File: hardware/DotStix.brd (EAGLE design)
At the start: 20.3 x 50 mm, 27 parts, among them IC2 SI1145, U1 ATMEGA328P-MU-QFN32, U2 TMP102

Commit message: Draft : first routing
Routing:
- net +3V3: track 0.00 -> 114.3 mm, vias 0 -> 3
- net RSDO: track 0.00 -> 68.3 mm, vias 0 -> 4
- net RST: track 0.00 -> 65.2 mm, vias 0 -> 6
- net RIRQ: track 0.00 -> 61.9 mm, vias 0 -> 2
- net SDA: track 0.00 -> 42.4 mm, vias 0 -> 4
- net REED: track 0.00 -> 40.1 mm, vias 0 -> 3
- net RSDI: track 0.15 -> 38.1 mm, vias 0 -> 2
- net SCL: track 0.00 -> 28.7 mm, vias 0 -> 1
- net INT_MULTIPLE: track 0.00 -> 28.5 mm, vias 0 -> 2
- net MOSI: track 0.00 -> 21.1 mm, vias 0 -> 1
- net MISO: track 0.00 -> 19.7 mm, vias 0 -> 1
- net LIGHT_SENSE: track 0.00 -> 19.3 mm, vias 0 -> 1
- net RSCK: track 0.00 -> 18.9 mm, vias 0 -> 2
- net LIGHT_SENSE_ENA: track 0.00 -> 18.2 mm, vias 0 -> 1
- net SCK: track 0.00 -> 13.5 mm
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
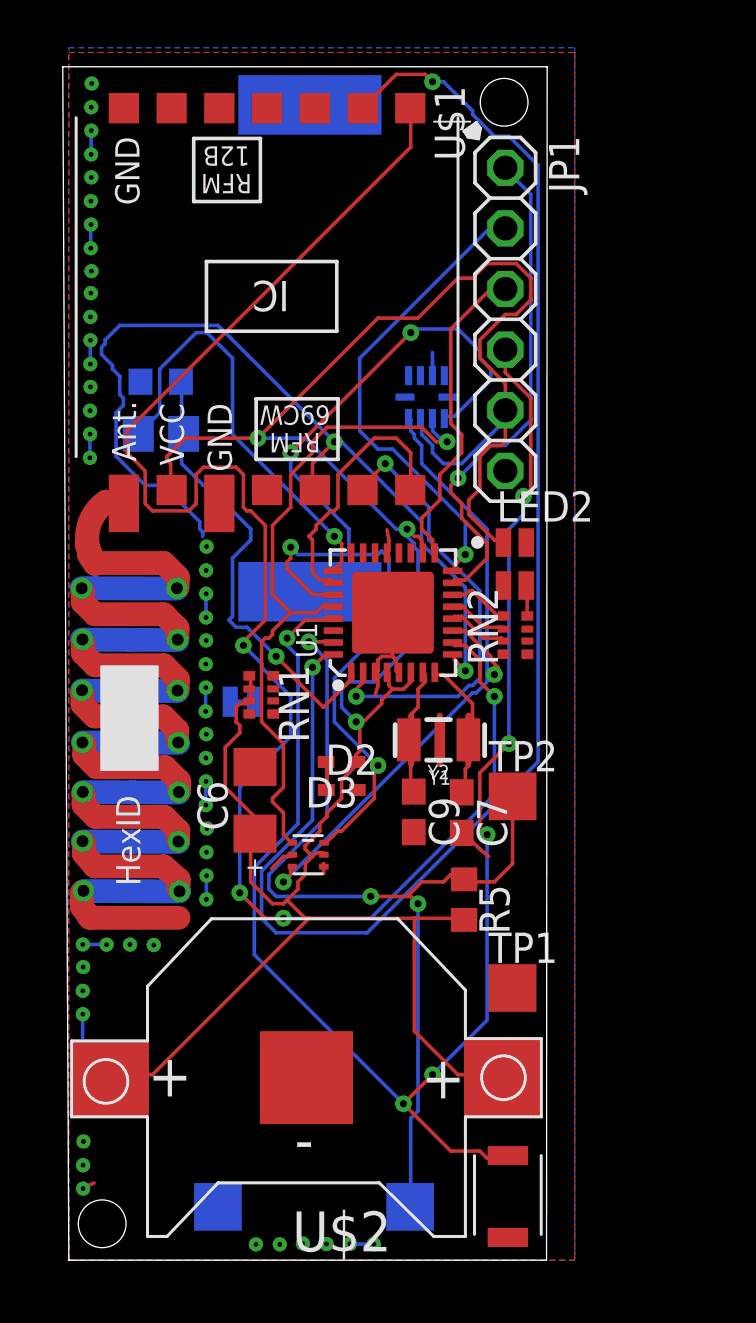
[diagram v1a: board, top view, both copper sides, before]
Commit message: Finished integration of Temp and UV sensors
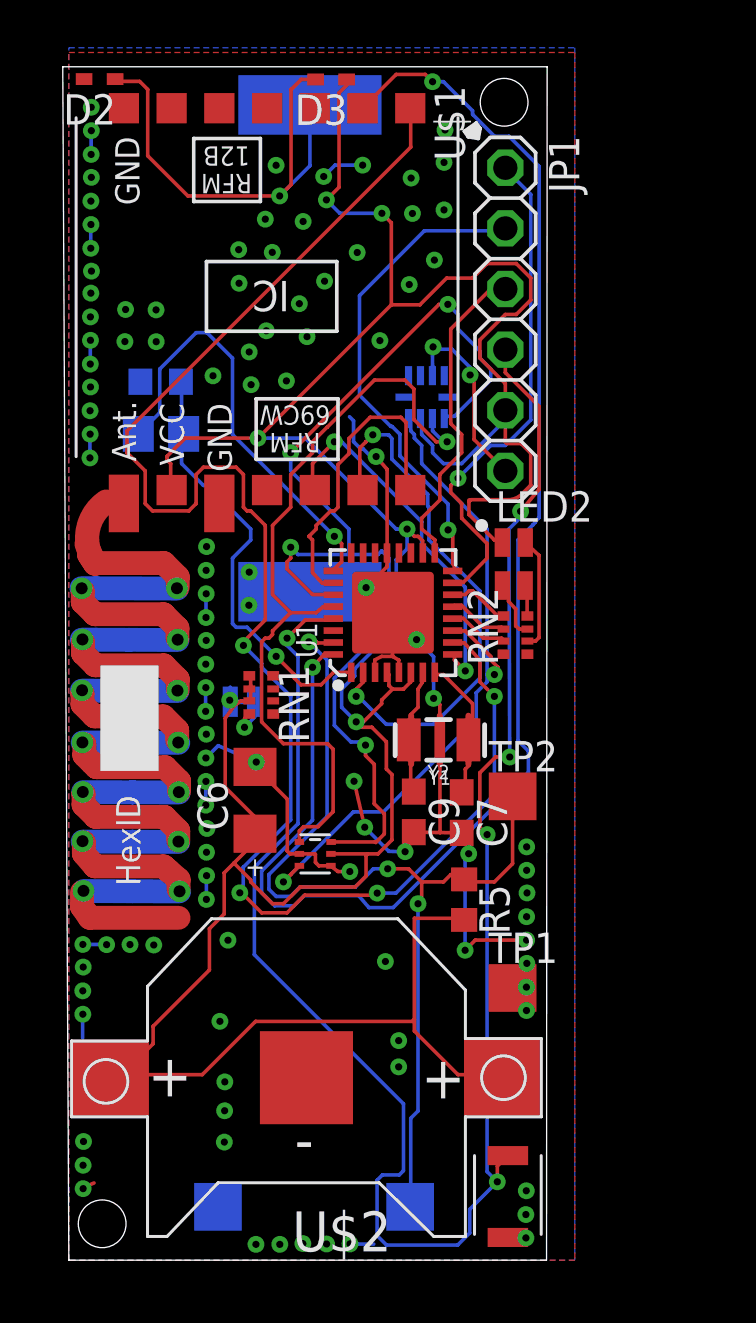
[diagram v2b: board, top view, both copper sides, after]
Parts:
- moved D2 31.4 mm to (1.34, 49.5), turned to 180 degrees
- moved D3 28.6 mm to (11.0, 49.5)
- moved U2 0.30 mm to (10.3, 17.0)
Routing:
- net GND: track 21.8 -> 71.1 mm, vias 49 -> 110
- net +3V3: track 114.3 -> 141.0 mm, vias 3 -> 6
- net RSDI: track 38.1 -> 15.4 mm
- net SOLAR_RAW: track 1.18 -> 20.8 mm, vias 0 -> 1
- net RST: track 65.2 -> 77.1 mm, vias 6 -> 5
- net N$4: track 0.00 -> 4.78 mm
- net SCL: track 28.7 -> 33.4 mm
- net RSCK: track 18.9 -> 22.7 mm
- net N$1: track 0.00 -> 2.47 mm
- net SDA: track 42.4 -> 44.8 mm
- net RSEL: track 11.3 -> 13.3 mm
- net N$5: track 0.00 -> 1.88 mm, vias 0 -> 1
- net REED: track 40.1 -> 41.0 mm
- net LIGHT_SENSE: track 19.3 -> 18.4 mm
- net MISO: track 19.7 -> 20.6 mm
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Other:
- board text removed: "Design rules : 100um width, 0.2mm vias"

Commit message: Move fast signals away from underneath XTAL
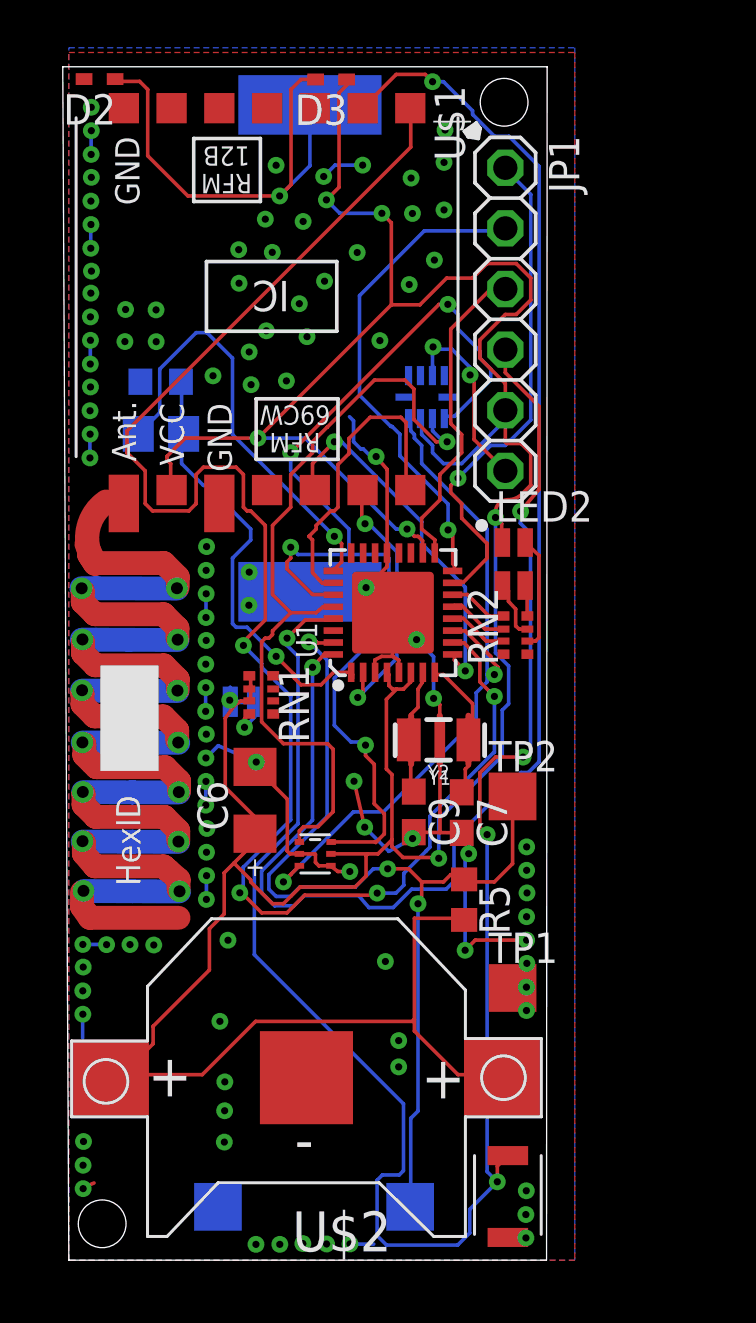
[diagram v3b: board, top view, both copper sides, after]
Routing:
- net RSCK: track 22.7 -> 11.4 mm
- net +3V3: track 141.0 -> 146.1 mm, vias 6 -> 7
- net RST: track 77.1 -> 77.9 mm
- net RIRQ: track 61.2 -> 61.9 mm

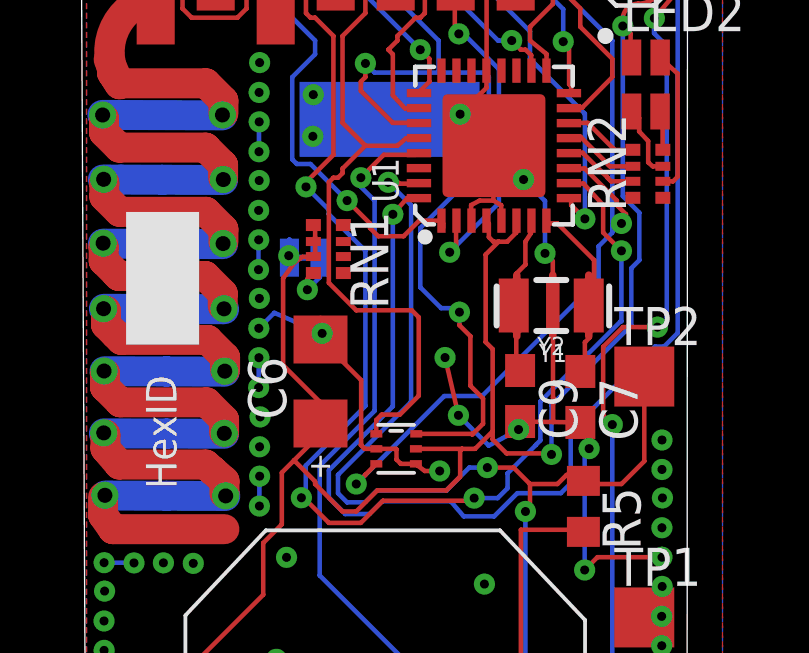
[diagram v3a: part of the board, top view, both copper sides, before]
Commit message: Fix unconnected 4.7k pullups
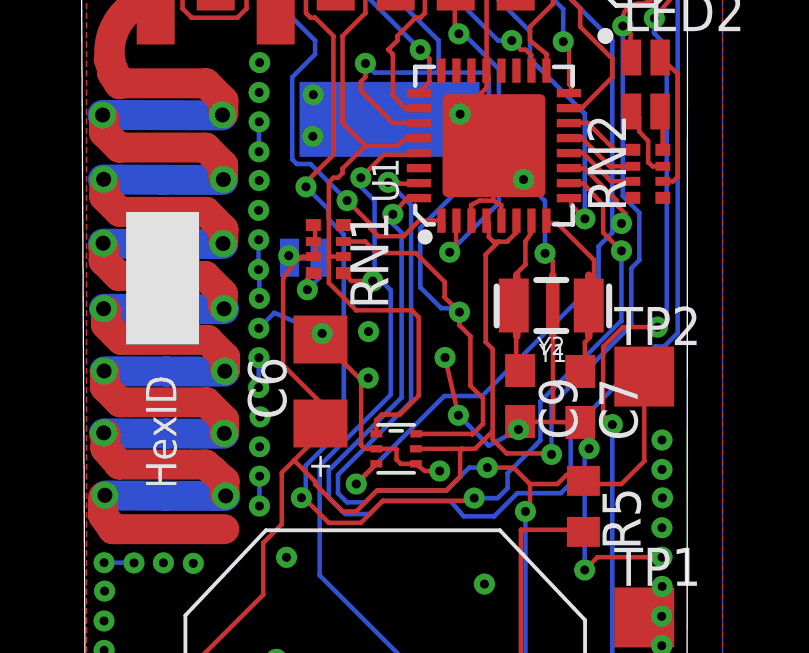
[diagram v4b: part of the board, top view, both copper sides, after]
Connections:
- net RST: now also RN1.1
- net SCL: now also RN1.2
- net SDA: now also RN1.3
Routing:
- net SDA: track 44.7 -> 49.8 mm
- net RST: track 77.9 -> 79.6 mm, vias 5 -> 6
- net +3V3: track 146.1 -> 144.9 mm
- net GND: track 70.9 -> 71.9 mm, vias 110 -> 112
- net RSDO: track 68.3 -> 67.8 mm
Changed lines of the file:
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@@
 <layer number="46" name="Milling" color="3" fill="1" visible="no" active="yes"/>
 <layer number="47" name="Measures" color="7" fill="1" visible="no" active="yes"/>
-<layer number="48" name="Document" color="7" fill="1" visible="yes" active="yes"/>
+<layer number="48" name="Document" color="7" fill="1" visible="no" active="yes"/>
 <layer number="49" name="Reference" color="7" fill="1" visible="no" active="yes"/>
 <layer number="50" name="dxf" color="7" fill="1" visible="no" active="no"/>
@@
 <via x="19.149059375" y="1.91261875" extent="1-16" drill="0.3"/>
 <via x="19.166840625" y="2.9083" extent="1-16" drill="0.3"/>
-<wire x1="5.760721875" y1="22.037040625" x2="5.73278125" y2="22.994621875" width="0" layer="19" extent="1-1"/>
+<wire x1="5.73278125" y1="22.994621875" x2="5.760721875" y2="22.994621875" width="0.1524" layer="16"/>
+<wire x1="5.760721875" y1="22.994621875" x2="5.760721875" y2="22.037040625" width="0.1524" layer="16"/>
+<via x="9.4005375" y="20.932140625" extent="1-16" drill="0.3"/>
+<via x="9.390378125" y="19.380203125" extent="1-16" drill="0.3"/>
 </signal>
 <signal name="SDA">
@@
 <wire x1="15.88008125" y1="40.04818125" x2="15.51178125" y2="40.04818125" width="0.1524" layer="1"/>
 <wire x1="13.2588" y1="29.5656" x2="13.4112" y2="29.4132" width="0.1524" layer="16"/>
+<contactref element="RN1" pad="3"/>
+<wire x1="8.5619625" y1="23.932959375" x2="9.2877" y2="23.932959375" width="0.1524" layer="1"/>
+<wire x1="9.2877" y1="23.932959375" x2="9.67231875" y2="23.548340625" width="0.1524" layer="1"/>
+<wire x1="9.67231875" y1="23.548340625" x2="10.977878125" y2="23.548340625" width="0.1524" layer="1"/>
+<wire x1="10.977878125" y1="23.548340625" x2="11.938" y2="22.58821875" width="0.1524" layer="1"/>
+<wire x1="11.938" y1="22.58821875" x2="11.938" y2="22.0726" width="0.1524" layer="1"/>
+<wire x1="11.938" y1="22.0726" x2="12.430759375" y2="21.579840625" width="0.1524" layer="1"/>
 </signal>
 <signal name="RST">
@@
 <wire x1="9.144" y1="25.7556" x2="9.144" y2="26.0604" width="0.1524" layer="16"/>
 <wire x1="9.6012" y1="25.2984" x2="9.144" y2="25.7556" width="0.1524" layer="16"/>
-<wire x1="9.6012" y1="18.288" x2="9.6012" y2="25.2984" width="0.1524" layer="16"/>
-<wire x1="7.7724" y1="16.4592" x2="9.6012" y2="18.288" width="0.1524" layer="16"/>
 <wire x1="7.7724" y1="12.8016" x2="7.7724" y2="16.4592" width="0.1524" layer="16"/>
 <wire x1="14.0208" y1="6.5532" x2="7.7724" y2="12.8016" width="0.1524" layer="16"/>
@@
 <wire x1="19.1389" y1="21.0693" x2="19.042378125" y2="21.0693" width="0.1524" layer="16"/>
 <wire x1="19.042378125" y1="21.0693" x2="19.03221875" y2="21.079459375" width="0.1524" layer="16"/>
+<contactref element="RN1" pad="1"/>
+<wire x1="7.7724" y1="16.4592" x2="10.14221875" y2="18.82901875" width="0.1524" layer="16"/>
+<wire x1="9.6012" y1="25.2984" x2="9.6012" y2="22.674578125" width="0.1524" layer="16"/>
+<wire x1="9.6012" y1="22.674578125" x2="9.54278125" y2="22.616159375" width="0.1524" layer="16"/>
+<via x="9.54278125" y="22.616159375" extent="1-16" drill="0.3"/>
+<wire x1="9.54278125" y1="22.616159375" x2="8.8287625" y2="22.616159375" width="0.1524" layer="1"/>
+<wire x1="8.8287625" y1="22.616159375" x2="8.5619625" y2="22.882959375" width="0.1524" layer="1"/>
+<wire x1="9.6012" y1="22.674578125" x2="9.776459375" y2="22.674578125" width="0.1524" layer="16"/>
+<wire x1="9.776459375" y1="22.674578125" x2="10.14221875" y2="22.30881875" width="0.1524" layer="16"/>
+<wire x1="10.14221875" y1="22.30881875" x2="10.14221875" y2="18.82901875" width="0.1524" layer="16"/>
 </signal>
 <signal name="RSEL">
@@
 <wire x1="17.2212" y1="24.2316" x2="17.2212" y2="25.146" width="0.1524" layer="1"/>
 <wire x1="17.8308" y1="23.622" x2="17.2212" y2="24.2316" width="0.1524" layer="1"/>
-<wire x1="8.0772" y1="24.8412" x2="9.2964" y2="23.622" width="0.1524" layer="16"/>
-<wire x1="8.0772" y1="24.9936" x2="8.0772" y2="24.8412" width="0.1524" layer="16"/>
 <wire x1="7.3152" y1="25.7556" x2="8.0772" y2="24.9936" width="0.1524" layer="16"/>
 <wire x1="7.3152" y1="25.908" x2="7.3152" y2="25.7556" width="0.1524" layer="1"/>
@@
 <via x="7.1628" y="15.3924" extent="1-16" drill="0.3"/>
 <via x="7.3152" y="25.7556" extent="1-16" drill="0.3"/>
-<wire x1="9.2964" y1="23.622" x2="9.2964" y2="18.4531" width="0.1524" layer="16"/>
-<wire x1="9.2964" y1="18.4531" x2="7.30758125" y2="16.46428125" width="0.1524" layer="16"/>
 <wire x1="7.30758125" y1="16.46428125" x2="7.30758125" y2="15.53718125" width="0.1524" layer="16"/>
 <wire x1="7.30758125" y1="15.53718125" x2="7.1628" y2="15.3924" width="0.1524" layer="16"/>
@@
 <wire x1="14.0335" y1="16.2052" x2="14.0335" y2="15.7099" width="0.1524" layer="16"/>
 <wire x1="14.0335" y1="15.7099" x2="13.7033" y2="15.3797" width="0.1524" layer="16"/>
+<wire x1="8.0772" y1="24.9936" x2="8.0772" y2="24.665940625" width="0.1524" layer="16"/>
+<wire x1="8.0772" y1="24.665940625" x2="8.57758125" y2="24.165559375" width="0.1524" layer="16"/>
+<wire x1="8.57758125" y1="24.165559375" x2="8.57758125" y2="17.73428125" width="0.1524" layer="16"/>
+<wire x1="8.57758125" y1="17.73428125" x2="7.30758125" y2="16.46428125" width="0.1524" layer="16"/>
 </signal>
 <signal name="RIRQ">
@@
 <wire x1="10.69848125" y1="25.389840625" x2="11.00328125" y2="25.389840625" width="0.1524" layer="1"/>
 <wire x1="10.2108" y1="24.8412" x2="10.69848125" y2="25.389840625" width="0.1524" layer="1"/>
-<wire x1="10.2108" y1="18.4404" x2="10.2108" y2="24.8412" width="0.1524" layer="16"/>
-<wire x1="8.0772" y1="16.3068" x2="10.2108" y2="18.4404" width="0.1524" layer="16"/>
+<wire x1="8.0772" y1="16.3068" x2="10.500359375" y2="18.729959375" width="0.1524" layer="16"/>
 <wire x1="18.4404" y1="47.0916" x2="19.70531875" y2="45.82668125" width="0.1524" layer="16"/>
 <wire x1="17.8308" y1="47.0916" x2="18.4404" y2="47.0916" width="0.1524" layer="16"/>
@@
 <wire x1="16.139159375" y1="17.625059375" x2="18.9484" y2="20.4343" width="0.1524" layer="16"/>
 <wire x1="18.9484" y1="20.4343" x2="19.255740625" y2="20.4343" width="0.1524" layer="16"/>
+<wire x1="10.2108" y1="24.8412" x2="10.2108" y2="24.51861875" width="0.1524" layer="16"/>
+<wire x1="10.2108" y1="24.51861875" x2="10.500359375" y2="24.229059375" width="0.1524" layer="16"/>
+<wire x1="10.500359375" y1="24.229059375" x2="10.500359375" y2="18.729959375" width="0.1524" layer="16"/>
 </signal>
 <signal name="+3V3">
@@
 <wire x1="6.72338125" y1="23.45181875" x2="6.741159375" y2="23.46198125" width="0.1524" layer="1"/>
 <via x="6.741159375" y="23.46198125" extent="1-16" drill="0.3"/>
-<wire x1="6.741159375" y1="23.46198125" x2="6.76401875" y2="24.0004625" width="0.1524" layer="16"/>
-<wire x1="6.76401875" y1="24.0004625" x2="6.76401875" y2="23.395940625" width="0.1524" layer="16"/>
 <wire x1="6.939278125" y1="23.238459375" x2="6.5532" y2="22.7076" width="0.1524" layer="1"/>
 <wire x1="18.288" y1="34.29" x2="18.361659375" y2="34.216340625" width="0.1524" layer="1"/>
@@
 <wire x1="15.49908125" y1="18.4785" x2="15.49908125" y2="16.837659375" width="0.1524" layer="16"/>
 <via x="15.49908125" y="16.837659375" extent="1-16" drill="0.3"/>
-<wire x1="15.49908125" y1="16.837659375" x2="15.453359375" y2="16.7919375" width="0" layer="19" extent="1-16"/>
-<wire x1="15.453359375" y1="16.7919375" x2="15.453359375" y2="16.5354" width="0" layer="19" extent="1-16"/>
 <wire x1="18.3896" y1="31.861759375" x2="17.87651875" y2="31.348678125" width="0.1524" layer="1" curve="90"/>
 <wire x1="17.87651875" y1="31.348678125" x2="17.87651875" y2="31.117540625" width="0.1524" layer="1"/>
@@
 <wire x1="14.00301875" y1="16.87068125" x2="15.466059375" y2="16.87068125" width="0.1524" layer="1"/>
 <wire x1="15.466059375" y1="16.87068125" x2="15.49908125" y2="16.837659375" width="0.1524" layer="1"/>
+<wire x1="6.741159375" y1="23.46198125" x2="6.76401875" y2="23.395940625" width="0" layer="19" extent="16-16"/>
 </signal>
 <signal name="MOSI">
@@
 <contactref element="U2" pad="1"/>
 <wire x1="8.0772" y1="22.5552" x2="8.9916" y2="21.6408" width="0.1524" layer="1"/>
-<wire x1="8.0772" y1="25.908" x2="8.0772" y2="22.5552" width="0.1524" layer="1"/>
+<wire x1="8.0772" y1="25.908" x2="8.0772" y2="23.432959375" width="0.1524" layer="1"/>
+<wire x1="8.0772" y1="23.276559375" x2="8.0772" y2="22.5552" width="0.1524" layer="1"/>
 <wire x1="8.2296" y1="26.0604" x2="8.0772" y2="25.908" width="0.1524" layer="1"/>
 <wire x1="8.382" y1="26.0604" x2="8.2296" y2="26.0604" width="0.1524" layer="1"/>
@@
 <wire x1="14.0817625" y1="36.87571875" x2="14.45768125" y2="36.4998" width="0.1524" layer="1"/>
 <wire x1="14.45768125" y1="36.4998" x2="14.45768125" y2="35.22471875" width="0.1524" layer="1"/>
+<contactref element="RN1" pad="2"/>
+<wire x1="8.5619625" y1="23.432959375" x2="8.0772" y2="23.432959375" width="0.1524" layer="1"/>
+<wire x1="8.0772" y1="23.432959375" x2="8.0772" y2="23.276559375" width="0.1524" layer="1"/>
 </signal>
 <signal name="ADC">
